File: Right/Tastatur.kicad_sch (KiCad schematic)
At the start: 66 parts, among them J101 Conn_02x05_Counter_Clockwise, J102 Conn_01x04_Pin, J103 XT60PW-M, Q101 SI2301CDS-T1-GE3, Q102 SI2301CDS-T1-GE3, Q103 SI2301CDS-T1-GE3, Q104 SI2301CDS-T1-GE3, Q105 SI2301CDS-T1-GE3, Q106 2N7002HW, Q107 SI2301CDS-T1-GE3, SW221 MK-12C02-G020, U101 USBLC6-2SC6, U102 CH592F, U103 AP2112K-3.3, U104 MT3608, U105 TP4056-42-ESOP8, U106 CD4052B, U107 LM393, Y101 32MHz

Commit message: update
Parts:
- removed J101: Conn_02x05_Counter_Clockwise, symbol Connector_Generic:Conn_02x05_Counter_Clockwise
- J102: renamed from J103; value XT60PW-M -> XT60PW-F; footprint Connector_AMASS:AMASS_XT60PW-M_1x02_P7.20mm_Horizontal -> Connector_AMASS:AMASS_XT60PW-F_1x02_P7.20mm_Horizontal
- renumbered H201 to H101, H202 to H102, J102 to J101, R205 to R101, R101 to R102, R102 to R103, R103 to R104, R104 to R105, R105 to R106, R106 to R107, R107 to R108, R108 to R109, R109 to R110, R110 to R111, R111 to R112, R112 to R113, R113 to R114, R114 to R115, SW221 to SW101, TP103 to TP102, TP104 to TP103
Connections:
- net GNDS is gone; now on net GND: AE101.2 (Shield)
- net +3V3: now also Q104.2 (S); no longer Q104.3 (D)
- net at J102.1 (Pin_1): now also Q104.3 (D); no longer Q104.2 (S)
- net MISO: no longer names the net of U102.25 (PA15)
- net MOSI: no longer names the net of U102.26 (PA14)
- net SCK: no longer names the net of U102.27 (PA13)
- no-connect marks 2 -> 5
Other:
- note removed: "ADNS"
- note removed: "Trackball Conn."
- moved on the sheet: Q104

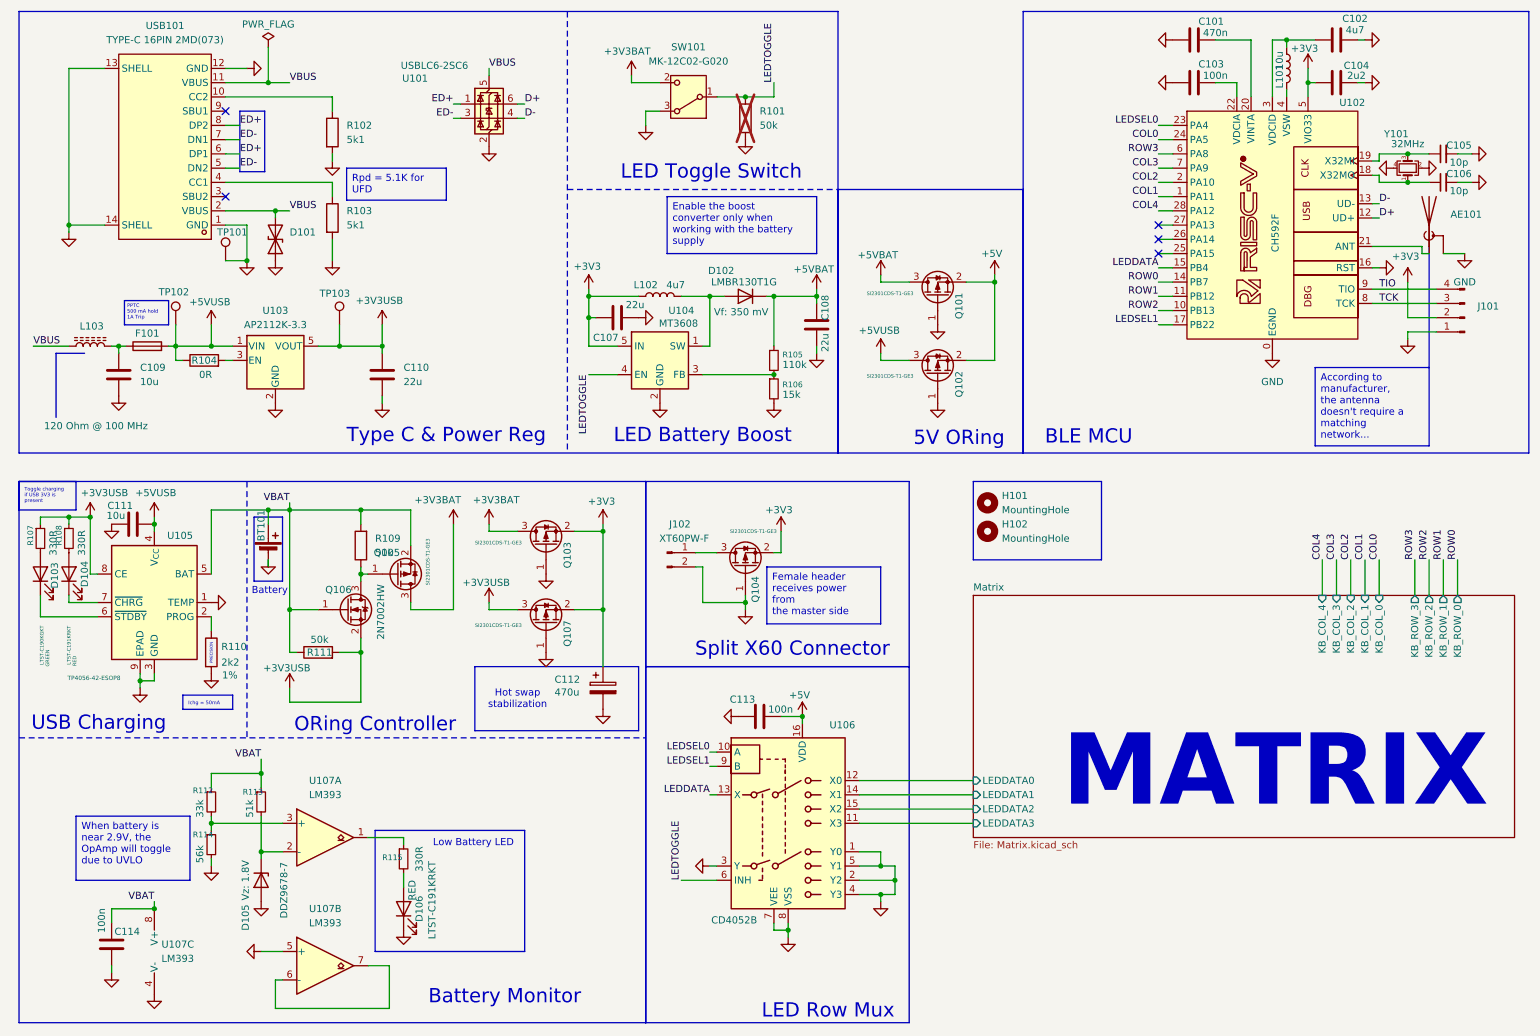
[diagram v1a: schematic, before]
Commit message: redesign with smaller components
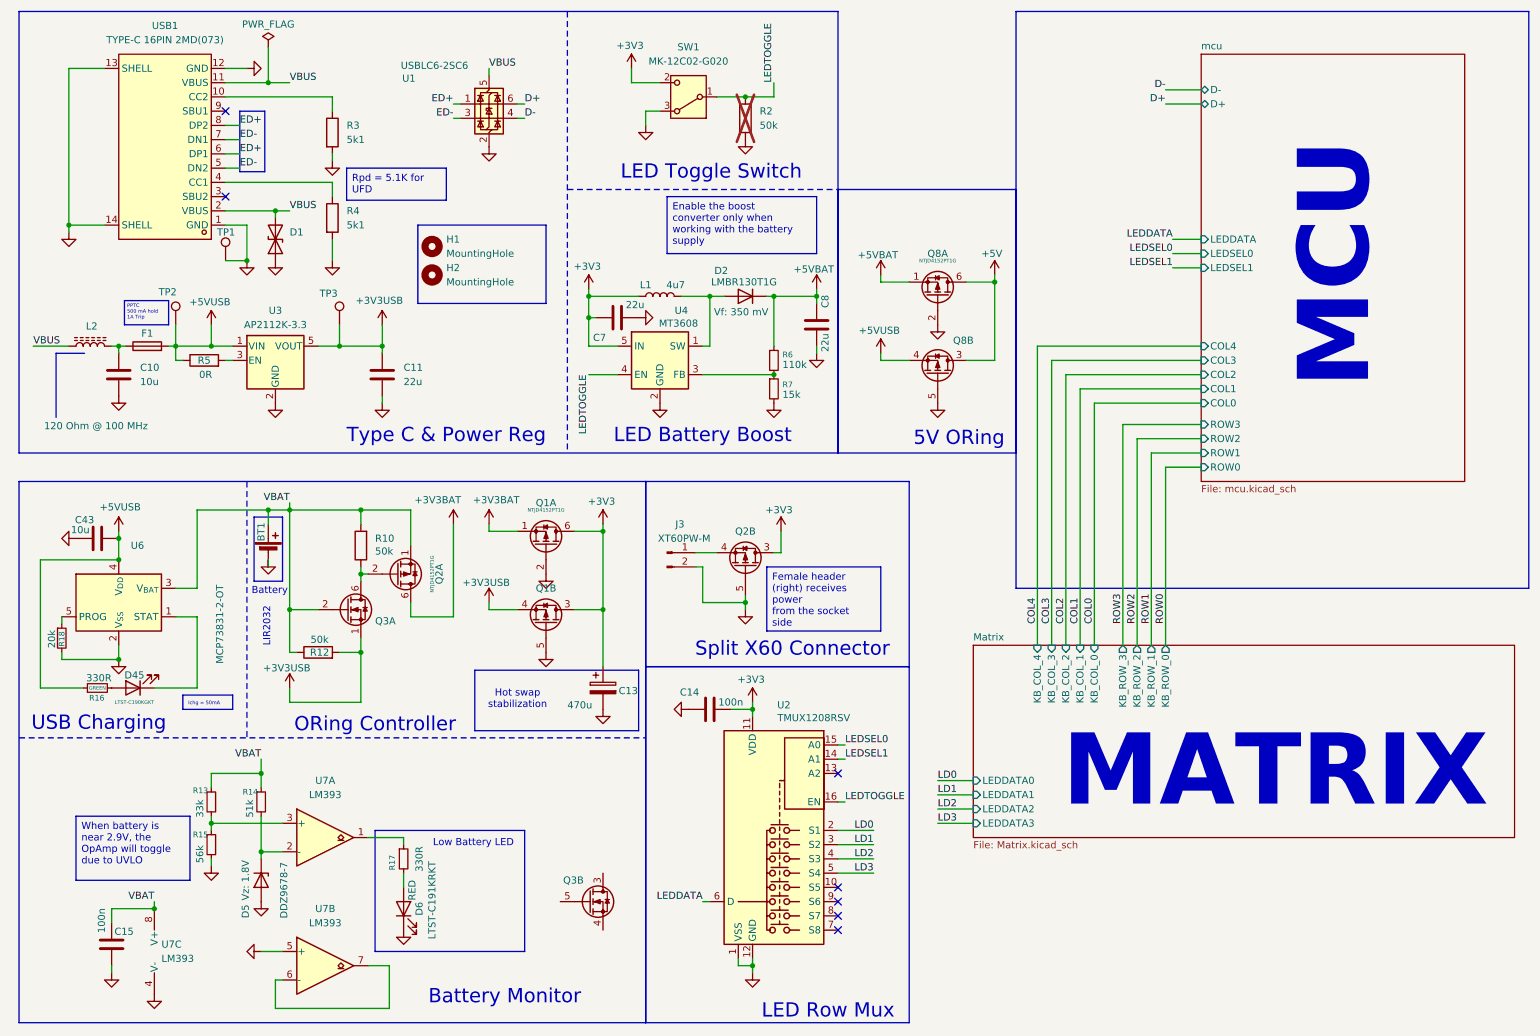
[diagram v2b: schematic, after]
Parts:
- removed AE101: Antenna_Shield, Inductor_SMD:L_1206_3216Metric, symbol Device:Antenna_Shield
- removed C101: 470n, Capacitor_SMD:C_0603_1608Metric_Pad1.08x0.95mm_HandSolder, symbol Device:C
- removed C102: 4u7, Capacitor_SMD:C_0603_1608Metric_Pad1.08x0.95mm_HandSolder, symbol Device:C
- removed C103: 100n, Capacitor_SMD:C_0603_1608Metric_Pad1.08x0.95mm_HandSolder, symbol Device:C
- removed C104: 2u2, Capacitor_SMD:C_0603_1608Metric_Pad1.08x0.95mm_HandSolder, symbol Device:C
- removed C105, C106: 10p, Capacitor_SMD:C_0603_1608Metric_Pad1.08x0.95mm_HandSolder, symbol Device:C_Small
- removed C111: 10u, Capacitor_SMD:C_0603_1608Metric_Pad1.08x0.95mm_HandSolder, symbol Device:C
- removed D103: GREEN, LED_SMD:LED_0603_1608Metric, symbol Device:LED
- removed D104: RED, LED_SMD:LED_0603_1608Metric, symbol Device:LED
- removed J101: Conn_01x04_Pin, Connector_JST:JST_PH_B4B-PH-K_1x04_P2.00mm_Vertical, symbol Connector:Conn_01x04_Pin
- removed L101: 10u, Inductor_SMD:L_0603_1608Metric_Pad1.05x0.95mm_HandSolder, symbol Device:L
- removed Q101, Q102, Q103, Q104, Q105, Q107: SI2301CDS-T1-GE3, Package_TO_SOT_SMD:SOT-23_Handsoldering, symbol Transistor_FET:Q_PMOS_GSD
- removed Q106: 2N7002HW, Package_TO_SOT_SMD:SOT-323_SC-70_Handsoldering, symbol Transistor_FET:2N7002H
- removed R107, R108: 330R, Resistor_SMD:R_0603_1608Metric_Pad0.98x0.95mm_HandSolder, symbol Device:R_Small
- removed R110: 2k2, Resistor_SMD:R_0603_1608Metric_Pad0.98x0.95mm_HandSolder, symbol Device:R
- removed U102: CH592F, steew:CH592F, symbol steew:CH592F
- removed U105: TP4056-42-ESOP8, Package_SO:SOP-8-1EP_4.57x4.57mm_P1.27mm_EP4.57x4.45mm, symbol Battery_Management:TP4056-42-ESOP8
- removed U106: CD4052B, Package_SO:TSSOP-16_4.4x5mm_P0.65mm, symbol Analog_Switch:CD4052B
- removed Y101: 32MHz, Crystal:Crystal_SMD_2016-4Pin_2.0x1.6mm, symbol Device:Crystal_GND24_Small
- added C43: 10u, Capacitor_SMD:C_0402_1005Metric_Pad0.74x0.62mm_HandSolder, symbol Device:C
- added D45: GREEN, LED_SMD:LED_0603_1608Metric, symbol Device:LED
- added Q1, Q2, Q8: NTJD4152PT1G, Package_TO_SOT_SMD:SOT-363_SC-70-6_Handsoldering, symbol Transistor_FET:Q_Dual_PMOS_S1G1D2S2G2D1
- added Q3: Q_Dual_NMOS_S1G1D2S2G2D1, Package_TO_SOT_SMD:SOT-363_SC-70-6, symbol Transistor_FET:Q_Dual_NMOS_S1G1D2S2G2D1
- added R16: 330R, Resistor_SMD:R_0402_1005Metric_Pad0.72x0.64mm_HandSolder, symbol Device:R_Small
- added R18: 20k, Resistor_SMD:R_0402_1005Metric_Pad0.72x0.64mm_HandSolder, symbol Device:R_Small
- added U2: TMUX1208RSV, Package_DFN_QFN:UQFN-16_1.8x2.6mm_P0.4mm, symbol Analog_Switch:TMUX1208RSV
- added U6: MCP73831-2-OT, Package_TO_SOT_SMD:SOT-23-5, symbol Battery_Management:MCP73831-2-OT
- C10: renamed from C109; footprint Capacitor_SMD:C_0603_1608Metric_Pad1.08x0.95mm_HandSolder -> Capacitor_SMD:C_0402_1005Metric_Pad0.74x0.62mm_HandSolder
- C11: renamed from C110; footprint Capacitor_SMD:C_0603_1608Metric_Pad1.08x0.95mm_HandSolder -> Capacitor_SMD:C_0402_1005Metric_Pad0.74x0.62mm_HandSolder
- C13: renamed from C112; footprint Capacitor_SMD:CP_Elec_6.3x7.7 -> Capacitor_Tantalum_SMD:CP_EIA-6032-28_Kemet-C_HandSolder
- C14: renamed from C113; footprint Capacitor_SMD:C_0603_1608Metric_Pad1.08x0.95mm_HandSolder -> Capacitor_SMD:C_0402_1005Metric_Pad0.74x0.62mm_HandSolder
- C15: renamed from C114; footprint Capacitor_SMD:C_0603_1608Metric_Pad1.08x0.95mm_HandSolder -> Capacitor_SMD:C_0402_1005Metric_Pad0.74x0.62mm_HandSolder
- C7: renamed from C107; footprint Capacitor_SMD:C_0603_1608Metric_Pad1.08x0.95mm_HandSolder -> Capacitor_SMD:C_0402_1005Metric_Pad0.74x0.62mm_HandSolder
- C8: renamed from C108; footprint Capacitor_SMD:C_0603_1608Metric_Pad1.08x0.95mm_HandSolder -> Capacitor_SMD:C_0402_1005Metric_Pad0.74x0.62mm_HandSolder
- J3: renamed from J102; value XT60PW-F -> XT60PW-M; footprint Connector_AMASS:AMASS_XT60PW-F_1x02_P7.20mm_Horizontal -> Connector_AMASS:AMASS_XT60PW-M_1x02_P7.20mm_Horizontal
- R10: renamed from R109; footprint Resistor_SMD:R_0603_1608Metric_Pad0.98x0.95mm_HandSolder -> Resistor_SMD:R_0402_1005Metric_Pad0.72x0.64mm_HandSolder
- R12: renamed from R111; footprint Resistor_SMD:R_0603_1608Metric_Pad0.98x0.95mm_HandSolder -> Resistor_SMD:R_0402_1005Metric_Pad0.72x0.64mm_HandSolder
- R13: renamed from R112; footprint Resistor_SMD:R_0603_1608Metric_Pad0.98x0.95mm_HandSolder -> Resistor_SMD:R_0402_1005Metric_Pad0.72x0.64mm_HandSolder
- R14: renamed from R113; footprint Resistor_SMD:R_0603_1608Metric_Pad0.98x0.95mm_HandSolder -> Resistor_SMD:R_0402_1005Metric_Pad0.72x0.64mm_HandSolder
- R15: renamed from R114; footprint Resistor_SMD:R_0603_1608Metric_Pad0.98x0.95mm_HandSolder -> Resistor_SMD:R_0402_1005Metric_Pad0.72x0.64mm_HandSolder
- R17: renamed from R115; footprint Resistor_SMD:R_0603_1608Metric_Pad0.98x0.95mm_HandSolder -> Resistor_SMD:R_0402_1005Metric_Pad0.72x0.64mm_HandSolder
- R2: renamed from R101; footprint Resistor_SMD:R_0603_1608Metric_Pad0.98x0.95mm_HandSolder -> Resistor_SMD:R_0402_1005Metric_Pad0.72x0.64mm_HandSolder
- R3: renamed from R102; footprint Resistor_SMD:R_0603_1608Metric_Pad0.98x0.95mm_HandSolder -> Resistor_SMD:R_0402_1005Metric_Pad0.72x0.64mm_HandSolder
- R4: renamed from R103; footprint Resistor_SMD:R_0603_1608Metric_Pad0.98x0.95mm_HandSolder -> Resistor_SMD:R_0402_1005Metric_Pad0.72x0.64mm_HandSolder
- R5: renamed from R104; footprint Resistor_SMD:R_0603_1608Metric_Pad0.98x0.95mm_HandSolder -> Resistor_SMD:R_0402_1005Metric_Pad0.72x0.64mm_HandSolder
- R6: renamed from R105; footprint Resistor_SMD:R_0603_1608Metric_Pad0.98x0.95mm_HandSolder -> Resistor_SMD:R_0402_1005Metric_Pad0.72x0.64mm_HandSolder
- R7: renamed from R106; footprint Resistor_SMD:R_0603_1608Metric_Pad0.98x0.95mm_HandSolder -> Resistor_SMD:R_0402_1005Metric_Pad0.72x0.64mm_HandSolder
- U7: renamed from U107; footprint Package_SO:SOIC-8_3.9x4.9mm_P1.27mm -> Package_DFN_QFN:DFN-8-1EP_2x2mm_P0.5mm_EP1.05x1.75mm; PN (none) -> LM393QT
- renumbered BT101 to BT1, D101 to D1, D102 to D2, D105 to D5, D106 to D6, F101 to F1, H101 to H1, H102 to H2, L102 to L1, L103 to L2, SW101 to SW1, TP101 to TP1, TP102 to TP2, TP103 to TP3, U101 to U1, U103 to U3, U104 to U4, USB101 to USB1
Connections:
- net +3V3: now also C14.1, SW1.2 (C), Q1.3 (D), Q1.6 (D), Q2.3 (D), U2.11 (VDD)
- net +3V3BAT: now also Q1.1 (S), Q2.6 (D); no longer SW1.2 (C)
- net +3V3USB: now also Q1.4 (S), Q3.1 (S)
- net +5V: now also Q8.3 (D), Q8.6 (D); no longer C14.1
- net +5VBAT: now also Q8.1 (S)
- net +5VUSB: now also C43.2, Q8.4 (S), R16.1, U6.4 (V_{DD})
- net GND: now also C43.1, Q1.2 (G), Q1.5 (G), Q2.5 (G), Q8.2 (G), Q8.5 (G), R18.2, U2.1 (VSS), U2.12 (GND), U6.2 (V_{SS})
- net LEDDATA: now also U2.6 (D)
- net LEDSEL0: now also U2.15 (A0)
- net LEDSEL1: now also U2.14 (A1)
- net LEDTOGGLE: now also U2.16 (EN)
- net VBAT: now also Q2.1 (S), Q3.2 (G), U6.3 (V_{BAT})
- net at J3.1 (Pin_1): now also Q2.4 (S)
- net at R10.1: now also Q2.2 (G), Q3.6 (D)
- new net: R18.1, U6.5 (PROG)
- new net: D45.1 (K), U6.1 (STAT)
- new net: D45.2 (A), R16.2
- new net LD0: U2.2 (S1)
- new net LD1: U2.3 (S2)
- new net LD2: U2.4 (S3)
- new net LD3: U2.5 (S4)
- no-connect marks 5 -> 7
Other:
- added sheet mcu (mcu.kicad_sch)
- note added: "LIR2032"
- note added: "MCU"
- note removed: "BLE MCU"
- note removed: "PRECISION"
- moved on the sheet: C14, H1, H2
